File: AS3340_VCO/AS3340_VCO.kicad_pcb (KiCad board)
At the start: 2 copper layers, 71.1 x 43.2 mm, 69 parts, among them J1 CV_In, J12 Conn_01x10, J2 Waveform_Out, U1 AS3340, U2 TL071, U4 TL071, U5 LM13700, U6 TL072

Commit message: AS3340_VCO rev 2 AS3310_ADSR rev 1 AS3320_VCF rev 1 AS3360_VCA rev 1 ER_Bus_Board rev 1
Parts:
- removed J12: Conn_01x10, Connector_IDC:IDC-Header_2x05_P2.54mm_Vertical
- added C7: 560pF, Capacitor_SMD:C_0805_2012Metric, F.Cu at (190.0, 93.2)
- added C8: 10uF, Capacitor_SMD:CP_Elec_4x3, F.Cu at (201.7, 73.4)
- added C9: 10uF, Capacitor_SMD:CP_Elec_4x3, F.Cu at (208.8, 73.4)
- added J3: Power, Connector_IDC:IDC-Header_2x08_P2.54mm_Vertical, B.Cu at (210.1, 69.6)
- added JP5: Jumper, Connector_PinHeader_2.54mm:PinHeader_1x02_P2.54mm_Vertical, B.Cu at (187.5, 89.4)
- added JP6: Jumper_3_Open, Connector_PinHeader_2.54mm:PinHeader_1x03_P2.54mm_Vertical, F.Cu at (143.5, 94.2)
- added R40: 47K, Resistor_SMD:R_0805_2012Metric, F.Cu at (175.2, 68.3)
- added R41: 100K, Resistor_SMD:R_0805_2012Metric, F.Cu at (159.0, 89.6)
- added R42: 1M, Resistor_SMD:R_0805_2012Metric, F.Cu at (162.3, 89.6)
- added R43: 100K 0.05%, Resistor_SMD:R_0805_2012Metric, F.Cu at (149.1, 89.8)
- added RV13: 100K, Potentiometer_THT:Potentiometer_Bourns_3296W_Vertical, B.Cu at (164.8, 81.3)
- added RV14: 10K, Potentiometer_THT:Potentiometer_Bourns_3296W_Vertical, B.Cu at (183.4, 68.3)
- added TP1: TestPoint, TestPoint:TestPoint_Pad_D2.0mm, B.Cu at (182.9, 83.8)
- added TP2: TestPoint, TestPoint:TestPoint_Pad_D2.0mm, B.Cu at (186.7, 83.8)
- R1, R2, R3: value 100K -> 100K 0.05%
- R13: value 1M -> 5.6K
- R14: value 360K -> 200K
- R21: value 1.5M -> 1.2M
- R4: value 24K -> 18K
- R6: value 1.8K -> 470
- RV1: value 10K -> 5K
- RV3: value 20K -> 1K
- U1, U5: footprint Package_SO:SOIC-16_3.9x9.9mm_P1.27mm -> Package_DIP:DIP-16_W7.62mm
- U2, U4, U6: footprint Package_SO:SOIC-8_3.9x4.9mm_P1.27mm -> Package_DIP:DIP-8_W7.62mm
- moved R38 140.6 mm to (232.4, 83.8), turned to 90 degrees
- moved R36 137.6 mm to (223.0, 72.1), turned to 180 degrees
- moved R34 136.7 mm to (217.9, 83.3)
- moved R39 136.2 mm to (232.4, 78.9)
- moved RV10 135.8 mm to (218.3, 81.0)
- moved R37 134.3 mm to (228.1, 88.1)
- moved U6 131.7 mm to (222.2, 74.9)
- moved R35 131.3 mm to (216.4, 73.9)
- moved RV11 130.0 mm to (229.6, 86.1), turned to 0 degrees
- moved R24 129.8 mm to (217.4, 100.1)
- moved J2 128.2 mm to (228.3, 65.5), turned to 270 degrees
- moved R23 127.2 mm to (217.5, 89.4)
- moved R25 124.1 mm to (222.3, 88.4)
- moved U4 123.6 mm to (222.0, 91.2)
- moved RV3 123.3 mm to (192.0, 98.6), turned to 0 degrees
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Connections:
- R13 pad 1: /Input Conditioning/CV -> /Vee
- R14 pad 1: +12V -> Net-(R14-Pad1)
- R21 pad 2: +12V -> Net-(R21-Pad2)
- R6 pad 1: GNDREF -> Net-(R6-Pad1)
- RV1 pad 2: /Vee -> Net-(R13-Pad2)
- RV1 pad 3: /Vee -> Net-(R13-Pad2)
- RV3 pad 1: GNDREF -> Net-(R6-Pad1)
- RV3 pad 2: Net-(R13-Pad2) -> GNDREF
- RV3 pad 3: /Input Conditioning/HFT -> GNDREF
- RV4 pad 2: /Input Conditioning/CV -> Net-(R41-Pad2)
- RV5 pad 2: /Input Conditioning/CV -> Net-(R42-Pad2)
- U1 pad 7: /Input Conditioning/HFT -> Net-(U1-Pad7)
- U2 pad 1: (no net) -> Net-(U2-Pad1)
- U2 pad 5: (no net) -> Net-(U2-Pad5)
- U2 pad 8: (no net) -> Net-(U2-Pad8)
- U4 pad 1: (no net) -> Net-(U4-Pad1)
- U4 pad 5: (no net) -> Net-(U4-Pad5)
- U4 pad 8: (no net) -> Net-(U4-Pad8)
- U5 pad 10: (no net) -> Net-(U5-Pad10)
- U5 pad 12: (no net) -> Net-(U5-Pad12)
- U5 pad 15: (no net) -> Net-(U5-Pad15)
- U5 pad 16: (no net) -> Net-(U5-Pad16)
- U5 pad 2: (no net) -> Net-(U5-Pad2)
- U5 pad 9: (no net) -> Net-(U5-Pad9)
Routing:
- net /Output Conditioning/TRI: track 18.6 -> 88.4 mm
- net /ER_CV: track 0.00 -> 62.2 mm
- net /Output Conditioning/RAW_PULSE: track 25.3 -> 80.7 mm
- net /Output Conditioning/RAW_SAW: track 11.7 -> 60.2 mm, vias 2 -> 1
- net Net-(C5-Pad1): track 3.59 -> 39.8 mm, vias 0 -> 2
- net /Output Conditioning/RAW_TRI: track 5.63 -> 41.1 mm
- net /Output Conditioning/SINE: track 8.03 -> 42.5 mm, vias 0 -> 1
- net /Input Conditioning/HFT: track 30.7 -> 0.00 mm
- net Net-(R4-Pad2): track 8.74 -> 32.2 mm
- net Net-(R9-Pad1): track 3.76 -> 23.0 mm
- net /Vee: track 15.4 -> 34.1 mm, vias 0 -> 1
- net /Input Conditioning/SOFT_SYNC: track 16.8 -> 35.2 mm
- net /Input Conditioning/CV: track 64.5 -> 46.4 mm, vias 0 -> 1
- net Net-(R5-Pad2): track 3.15 -> 20.7 mm, vias 0 -> 1
- net Net-(C7-Pad2): track 2.83 -> 18.9 mm
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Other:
- board size 71.1 x 43.2 mm -> 96.5 x 38.1 mm
- board text added: "Pulse Offset"
- board text added: "Ref Pitch"
- board text added: "Refind"
- board text added: "Saw Offset"
- board text added: "Tempco Adj"
- board text added: "Tri Offset"
- board text added: "VCO Board Rev 2"
- board text added: "WHSynth"
- board text removed: "HFT"
- board text removed: "Pulse Level"
- board text removed: "Saw Level"
- board text removed: "Tri Level"

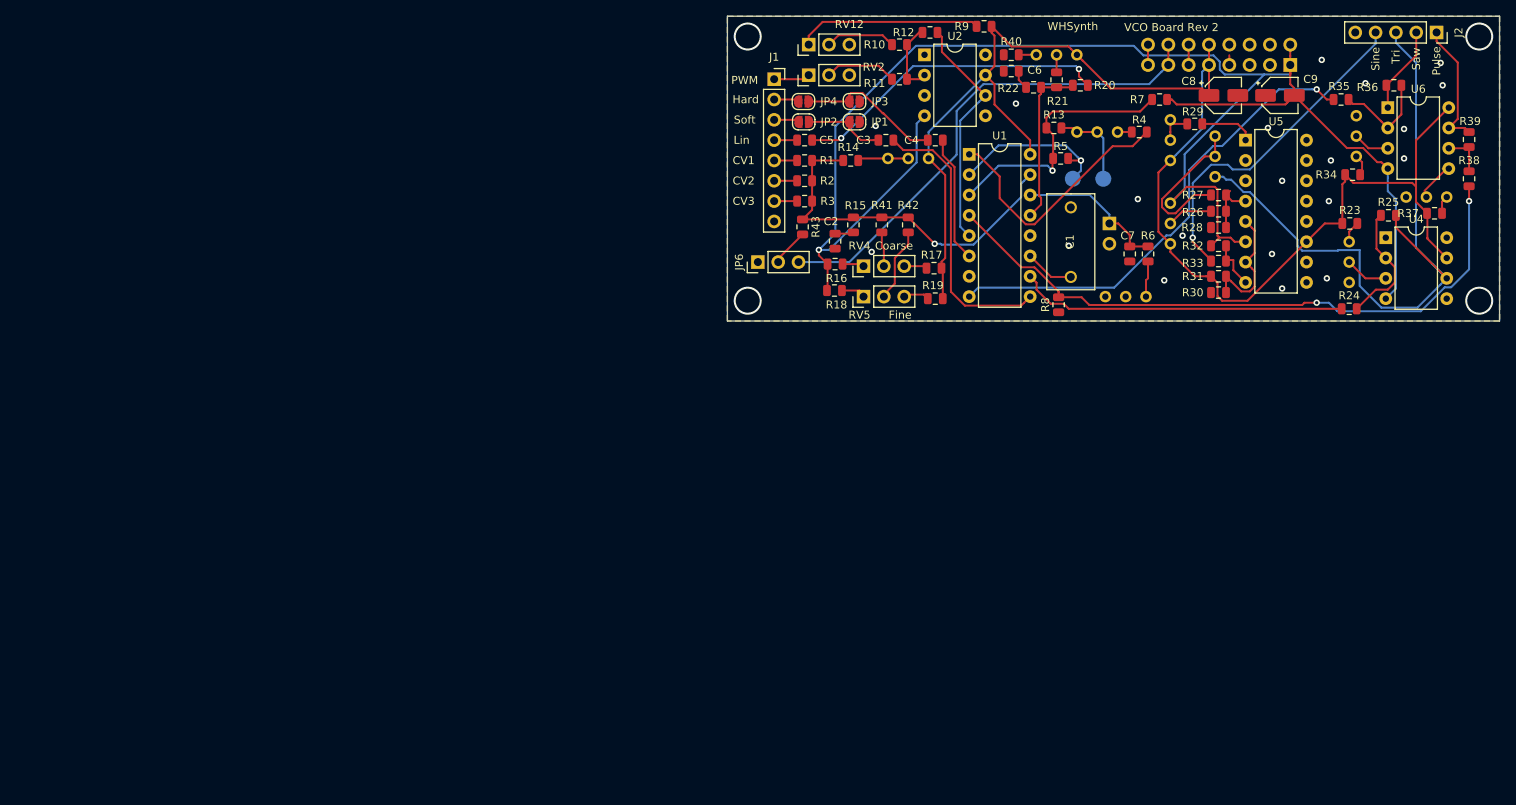
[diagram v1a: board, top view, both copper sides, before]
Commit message: Re-do VCO board to support new front panel board
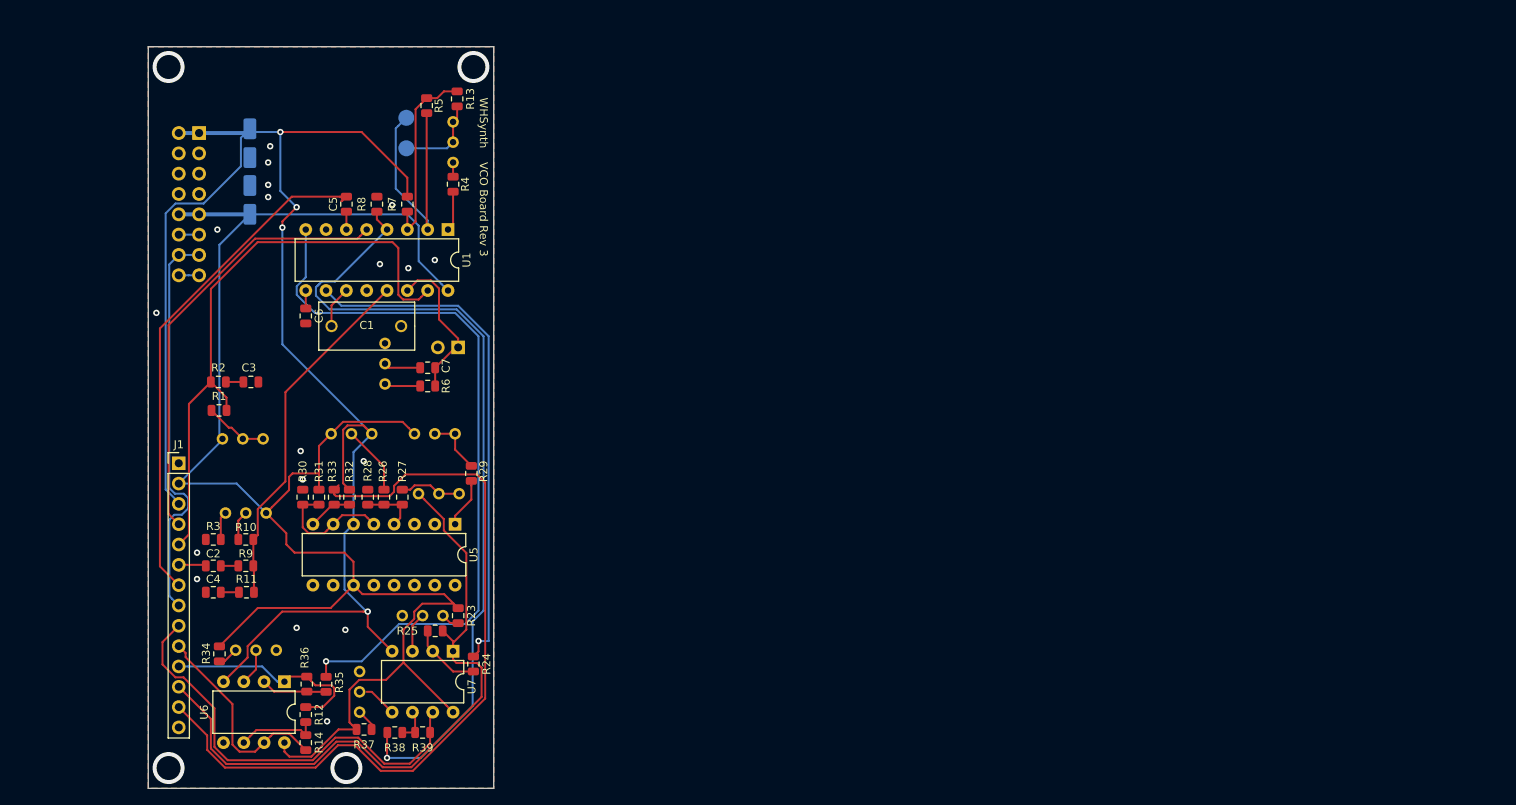
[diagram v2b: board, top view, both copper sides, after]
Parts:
- removed J2: Waveform_Out, Connector_PinSocket_2.54mm:PinSocket_1x05_P2.54mm_Vertical
- removed JP1: Soft_Sync_Bypass, Jumper:SolderJumper-2_P1.3mm_Open_RoundedPad1.0x1.5mm
- removed JP2: Soft_Sync, Jumper:SolderJumper-2_P1.3mm_Open_RoundedPad1.0x1.5mm
- removed JP3: Hard_Sync_Bypass, Jumper:SolderJumper-2_P1.3mm_Open_RoundedPad1.0x1.5mm
- removed JP4: Hard_Sync, Jumper:SolderJumper-2_P1.3mm_Open_RoundedPad1.0x1.5mm
- removed JP6: Jumper_3_Open, Connector_PinHeader_2.54mm:PinHeader_1x03_P2.54mm_Vertical
- removed R15, R22: 470, Resistor_SMD:R_0805_2012Metric
- removed R16, R17: 200K, Resistor_SMD:R_0805_2012Metric
- removed R18: 10K, Resistor_SMD:R_0805_2012Metric
- removed R19, R40: 47K, Resistor_SMD:R_0805_2012Metric
- removed R20, R42: 1M, Resistor_SMD:R_0805_2012Metric
- removed R21: 1.2M, Resistor_SMD:R_0805_2012Metric
- removed R41: 100K, Resistor_SMD:R_0805_2012Metric
- removed R43: 100K 0.05%, Resistor_SMD:R_0805_2012Metric
- removed RV12, RV5: 100K, Connector_PinHeader_2.54mm:PinHeader_1x03_P2.54mm_Vertical
- removed RV13: 100K, Potentiometer_THT:Potentiometer_Bourns_3296W_Vertical
- removed RV14: 10K, Potentiometer_THT:Potentiometer_Bourns_3296W_Vertical
- removed U2, U4: TL071, Package_DIP:DIP-8_W7.62mm
- added U7: TL072, Package_DIP:DIP-8_W7.62mm, F.Cu at (105.4, 142.9)
- C2: value 10nF -> 100nF
- C3, C4: value 1nF -> 10nF
- C5: value 100nF -> 1nF
- C6: value 10nF -> 1nF
- C8, C9: moved to B.Cu
- J1: value CV_In -> Conn_01x14; footprint Connector_PinSocket_2.54mm:PinSocket_1x08_P2.54mm_Vertical -> Connector_PinHeader_2.54mm:PinHeader_1x14_P2.54mm_Vertical
- R1: value 100K 0.05% -> 100K
- R10: value 100K -> 1.2M
- R11: value 100K -> 470
- R12: value 100K -> 10K
- R14: value 200K -> 10K
- R2: value 100K 0.05% -> 470
- R3: value 100K 0.05% -> 22K
- R6: value 470 -> 1K
- R9: value 200K -> 1M
- RV2: value 100K -> 10K; footprint Connector_PinHeader_2.54mm:PinHeader_1x03_P2.54mm_Vertical -> Potentiometer_THT:Potentiometer_Bourns_3296W_Vertical; moved to B.Cu
- RV4: footprint Connector_PinHeader_2.54mm:PinHeader_1x03_P2.54mm_Vertical -> Potentiometer_THT:Potentiometer_Bourns_3296W_Vertical; moved to B.Cu
- moved U6 155.5 mm to (84.3, 146.7), turned to 270 degrees
- moved R36 155.1 mm to (87.1, 147.0), turned to 90 degrees
- moved R34 153.8 mm to (76.2, 143.2), turned to 270 degrees
- moved RV10 153.1 mm to (78.2, 142.7), turned to 180 degrees
- moved R38 151.1 mm to (98.1, 153.0), turned to 0 degrees
- moved RV11 150.4 mm to (93.7, 150.5), turned to 270 degrees
- moved R39 150.3 mm to (101.6, 153.0), turned to 0 degrees
- moved R37 148.6 mm to (94.3, 152.7)
- moved R35 146.4 mm to (89.5, 147.0), turned to 270 degrees
- moved J3 136.7 mm to (73.7, 78.1), turned to 180 degrees
- moved R25 130.0 mm to (103.2, 140.3)
- moved C9 128.9 mm to (80.0, 79.4), turned to 90 degrees
- moved RV6 122.5 mm to (104.1, 138.4), turned to 0 degrees
- moved C8 122.4 mm to (80.0, 86.5), turned to 90 degrees
- moved R23 121.8 mm to (106.0, 138.4), turned to 270 degrees
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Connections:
- net /ER_GATE renamed /REAR_GATE
- net /Output Conditioning/RAW_SAW renamed /Output Conditioning/RAW_RAMP
- C2 pad 1: GNDREF -> Net-(C2-Pad1)
- C2 pad 2: Net-(C2-Pad2) -> /LIN
- C3 pad 1: /Input Conditioning/SOFT_SYNC -> GNDREF
- C4 pad 1: /Input Conditioning/HARD_SYNC -> GNDREF
- C5 pad 2: /Input Conditioning/LIN_RAW -> /SYNC
- C6 pad 1: GNDREF -> Net-(C6-Pad1)
- C6 pad 2: Net-(C6-Pad2) -> GNDREF
- J1 pad 1: /Input Conditioning/PWM_RAW -> GNDREF
- J1 pad 2: /Input Conditioning/HARD_SYNC_RAW -> +12V
- J1 pad 3: /Input Conditioning/SOFT_SYNC_RAW -> -12V
- J1 pad 4: /Input Conditioning/LIN_RAW -> /PWM
- J1 pad 5: Net-(J1-Pad5) -> /CV
- J1 pad 6: Net-(J1-Pad6) -> /LIN
- J1 pad 7: Net-(J1-Pad7) -> /SYNC
- J1 pad 8: GNDREF -> /REAR_CV
- J3 pad 13: /ER_CV -> /REAR_CV
- J3 pad 14: /ER_CV -> /REAR_CV
- R1 pad 1: /Input Conditioning/CV -> /CV
- R1 pad 2: Net-(J1-Pad5) -> Net-(R1-Pad2)
- R11 pad 1: Net-(R10-Pad1) -> Net-(C4-Pad2)
- R11 pad 2: Net-(R11-Pad2) -> Net-(R10-Pad1)
- R12 pad 1: /Input Conditioning/PWM -> /Saw
- R12 pad 2: Net-(R10-Pad1) -> Net-(R12-Pad2)
- R14 pad 1: Net-(R14-Pad1) -> Net-(R12-Pad2)
- R14 pad 2: /Input Conditioning/CV -> /Ramp
- R2 pad 1: /Input Conditioning/CV -> Net-(C3-Pad2)
- R2 pad 2: Net-(J1-Pad6) -> /CV
- R25 pad 2: /Output Conditioning/TRI -> /Tri
- R3 pad 1: /Input Conditioning/CV -> GNDREF
- R3 pad 2: Net-(J1-Pad7) -> Net-(R3-Pad2)
- R33 pad 2: /Output Conditioning/SINE -> /Sine
- R36 pad 2: /Output Conditioning/SAW -> /Saw
- R39 pad 2: /Output Conditioning/PULSE -> /Pulse
- R9 pad 1: Net-(R9-Pad1) -> Net-(R10-Pad1)
- R9 pad 2: +12V -> Net-(C2-Pad1)
- RV2 pad 1: /Input Conditioning/PWM_RAW -> +12V
- RV2 pad 2: Net-(R11-Pad2) -> Net-(R10-Pad2)
- RV2 pad 3: GNDREF -> Net-(R3-Pad2)
- RV4 pad 1: Net-(R16-Pad1) -> +12V
- RV4 pad 2: Net-(R41-Pad2) -> Net-(R1-Pad2)
- RV4 pad 3: Net-(R17-Pad2) -> Net-(R1-Pad2)
- RV7 pad 1: /Output Conditioning/TRI -> /Tri
- U1 pad 13: /Input Conditioning/LIN -> Net-(R10-Pad1)
- U1 pad 15: /Input Conditioning/CV -> /CV
- U1 pad 5: /Input Conditioning/PWM -> /PWM
- U1 pad 6: /Input Conditioning/HARD_SYNC -> Net-(C5-Pad1)
- U1 pad 9: /Input Conditioning/SOFT_SYNC -> Net-(C6-Pad1)
- U6 pad 1: /Output Conditioning/SAW -> /Saw
- U6 pad 5: Net-(RV11-Pad2) -> GNDREF
- U6 pad 6: Net-(R38-Pad2) -> Net-(R12-Pad2)
- U6 pad 7: /Output Conditioning/PULSE -> /Ramp
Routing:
- net /Sine: track 0.00 -> 98.0 mm
- net /Output Conditioning/TRI: track 88.4 -> 0.00 mm
- net /Tri: track 0.00 -> 84.8 mm
- net /CV: track 0.00 -> 74.4 mm
- net /SYNC: track 0.00 -> 64.1 mm
- net /ER_CV: track 62.2 -> 0.00 mm
- net /PWM: track 0.00 -> 55.1 mm
- net /Pulse: track 0.00 -> 55.1 mm
- net /REAR_CV: track 0.00 -> 50.5 mm
- net /Input Conditioning/CV: track 46.4 -> 0.00 mm, vias 1 -> 0
- net /Output Conditioning/SINE: track 42.5 -> 0.00 mm, vias 1 -> 0
- net Net-(C5-Pad1): track 39.8 -> 2.24 mm, vias 2 -> 0
- net Net-(R10-Pad1): track 9.28 -> 44.7 mm
- net /Input Conditioning/SOFT_SYNC: track 35.2 -> 0.00 mm
- net +12V: track 181.5 -> 216.6 mm
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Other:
- board size 96.5 x 38.1 mm -> 43.2 x 92.7 mm
- board text added: "+12"
- board text added: "-12"
- board text added: "CV"
- board text added: "GND"
- board text added: "Ramp"
- board text added: "Rear"
- board text added: "Sync"
- board text added: "VCO Board Rev 3"
- board text removed: "CV1"
- board text removed: "CV2"
- board text removed: "CV3"
- board text removed: "Coarse"
- board text removed: "Fine"
- board text removed: "Hard"
- board text removed: "Soft"
- board text removed: "VCO Board Rev 2"
